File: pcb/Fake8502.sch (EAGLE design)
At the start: 16 parts, among them IC2 XC9572XLTQG100, IC5 HDR, IC6 65(C)02

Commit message: Fixed port definitions
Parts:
- removed IC5: HDR, commodore:8502-RP
- removed IC6: 65(C)02, commodore:6502-RP
- added IC1: W65C02SP, commodore:W65C02SP-R
- added IC3: XC9572XLTQG100, xilinx_xc95XXXxl:XC9572XLTQG100
- added SJ1: (no value), jumper:SJ
- IC2: value XC9572XLTQG100 -> MOS8502; device xilinx_xc95XXXxl:XC9572XLTQG100 -> commodore:8502-RP
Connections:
- removed net !RDY': IC2.FB1MC15, IC6A.!RDY
- new net N$1: IC1A.!VP, SJ1.2
- net !IRQ: now also IC1A.!IRQ, IC2>NAME.!IRQ, IC3.FB1MC17; no longer IC2.FB1MC17, IC5>NAME.!IRQ, IC6A.!IRQ
- net !NMI: now also IC1A.!NMI, IC2>NAME.!NMI, IC3.FB3MC2; no longer IC2.FB3MC2, IC5>NAME.!NMI, IC6A.!NMI
- net !RDY: now also IC1A.!RDY, IC2>NAME.!RDY, IC3.FB1MC10; no longer IC2.FB1MC10, IC5>NAME.!RDY
- net !RESET: now also IC1A.!RESET, IC2>NAME.!RESET, IC3.FB2MC9-I/O/GSR; no longer IC2.FB2MC9-I/O/GSR, IC5>NAME.!RESET, IC6A.!RESET
- net +3V3: now also IC3.VCCINT3,3V@1, IC3.VCCINT3,3V@2, IC3.VCCINT3,3V@3, IC3.VCCIO2,5V/3,3V@1, IC3.VCCIO2,5V/3,3V@2, IC3.VCCIO2,5V/3,3V@3, IC3.VCCIO2,5V/3,3V@4; no longer IC2.VCCINT3,3V@1, IC2.VCCINT3,3V@2, IC2.VCCINT3,3V@3, IC2.VCCIO2,5V/3,3V@1, IC2.VCCIO2,5V/3,3V@2, IC2.VCCIO2,5V/3,3V@3, IC2.VCCIO2,5V/3,3V@4
- net A'0: now also IC1A.A0, IC3.FB1MC4; no longer IC2.FB1MC4, IC6A.A0
- net A'1: now also IC1A.A1, IC3.FB1MC8; no longer IC2.FB1MC8, IC6A.A1
- net A'10: now also IC1A.A10, IC3.FB3MC15; no longer IC2.FB3MC15, IC6A.A10
- net A'11: now also IC1A.A11, IC3.FB3MC18; no longer IC2.FB3MC18, IC6A.A11
- net A'12: now also IC1A.A12, IC3.FB4MC3; no longer IC2.FB4MC3, IC6A.A12
- net A'13: now also IC1A.A13, IC3.FB4MC11; no longer IC2.FB4MC11, IC6A.A13
- net A'14: now also IC1A.A14, IC3.FB4MC7; no longer IC2.FB4MC7, IC6A.A14
- net A'15: now also IC1A.A15, IC3.FB4MC18; no longer IC2.FB4MC18, IC6A.A15
- net A'2: now also IC1A.A2, IC3.FB1MC6; no longer IC2.FB1MC6, IC6A.A2
- net A'3: now also IC1A.A3, IC3.FB1MC12; no longer IC2.FB1MC12, IC6A.A3
- net A'4: now also IC1A.A4, IC3.FB1MC13; no longer IC2.FB1MC13, IC6A.A4
- net A'5: now also IC1A.A5, IC3.FB1MC16; no longer IC2.FB1MC16, IC6A.A5
- net A'6: now also IC1A.A6, IC3.FB3MC1; no longer IC2.FB3MC1, IC6A.A6
- net A'7: now also IC1A.A7, IC3.FB3MC3; no longer IC2.FB3MC3, IC6A.A7
- net A'8: now also IC1A.A8, IC3.FB3MC11; no longer IC2.FB3MC11, IC6A.A8
- net A'9: now also IC1A.A9, IC3.FB3MC7; no longer IC2.FB3MC7, IC6A.A9
- net A0: now also IC2>NAME.A0, IC3.FB1MC10-I/O/GCK2; no longer IC2.FB1MC10-I/O/GCK2, IC5>NAME.A0
- net A1: now also IC2>NAME.A1, IC3.FB1MC9-I/O/GCK1; no longer IC2.FB1MC9-I/O/GCK1, IC5>NAME.A1
- net A10: now also IC2>NAME.A10, IC3.FB3MC6; no longer IC2.FB3MC6, IC5>NAME.A10
- net A11: now also IC2>NAME.A11, IC3.FB3MC14; no longer IC2.FB3MC14, IC5>NAME.A11
- net A12: now also IC2>NAME.A12, IC3.FB3MC17; no longer IC2.FB3MC17, IC5>NAME.A12
- net A13: now also IC2>NAME.A13, IC3.FB3MC10; no longer IC2.FB3MC10, IC5>NAME.A13
- net A14: now also IC2>NAME.A14, IC3.FB4MC4; no longer IC2.FB4MC4, IC5>NAME.A14
- net A15: now also IC2>NAME.A15, IC3.FB4MC6; no longer IC2.FB4MC6, IC5>NAME.A15
- net A2: now also IC2>NAME.A2, IC3.FB1MC3; no longer IC2.FB1MC3, IC5>NAME.A2
- net A3: now also IC2>NAME.A3, IC3.FB1MC1; no longer IC2.FB1MC1, IC5>NAME.A3
- net A4: now also IC2>NAME.A4, IC3.FB1MC5; no longer IC2.FB1MC5, IC5>NAME.A4
- net A5: now also IC2>NAME.A5, IC3.FB3MC5; no longer IC2.FB3MC5, IC5>NAME.A5
- net A6: now also IC2>NAME.A6, IC3.FB3MC8; no longer IC2.FB3MC8, IC5>NAME.A6
- net A7: now also IC2>NAME.A7, IC3.FB1MC18; no longer IC2.FB1MC18, IC5>NAME.A7
- net A8: now also IC2>NAME.A8, IC3.FB3MC9; no longer IC2.FB3MC9, IC5>NAME.A8
- net A9: now also IC2>NAME.A9, IC3.FB3MC4; no longer IC2.FB3MC4, IC5>NAME.A9
- net AEC: now also IC2>NAME.AEC, IC3.FB1MC7; no longer IC2.FB1MC7, IC5>NAME.AEC
- net D'0: now also IC1A.D0, IC3.FB2MC13; no longer IC2.FB2MC13, IC6A.D0
- net D'1: now also IC1A.D1, IC3.FB2MC16; no longer IC2.FB2MC16, IC6A.D1
- net D'2: now also IC1A.D2, IC3.FB2MC17; no longer IC2.FB2MC17, IC6A.D2
- net D'3: now also IC1A.D3, IC3.FB2MC4; no longer IC2.FB2MC4, IC6A.D3
- net D'4: now also IC1A.D4, IC3.FB2MC3; no longer IC2.FB2MC3, IC6A.D4
- net D'5: now also IC1A.D5, IC3.FB4MC15; no longer IC2.FB4MC15, IC6A.D5
- net D'6: now also IC1A.D6, IC3.FB4MC16; no longer IC2.FB4MC16, IC6A.D6
- net D'7: now also IC1A.D7, IC3.FB4MC12; no longer IC2.FB4MC12, IC6A.D7
- net D0: now also IC2>NAME.D0, IC3.FB2MC6; no longer IC2.FB2MC6, IC5>NAME.D0
- net D1: now also IC2>NAME.D1, IC3.FB2MC5; no longer IC2.FB2MC5, IC5>NAME.D1
- net D2: now also IC2>NAME.D2, IC3.FB2MC2; no longer IC2.FB2MC2, IC5>NAME.D2
- net D3: now also IC2>NAME.D3, IC3.FB2MC10; no longer IC2.FB2MC10, IC5>NAME.D3
- net D4: now also IC2>NAME.D4, IC3.GTS1; no longer IC2.GTS1, IC5>NAME.D4
- net D5: now also IC2>NAME.D5, IC3.FB2MC12; no longer IC2.FB2MC12, IC5>NAME.D5
- net D6: now also IC2>NAME.D6, IC3.FB2MC14; no longer IC2.FB2MC14, IC5>NAME.D6
- net D7: now also IC2>NAME.D7, IC3.FB2MC15; no longer IC2.FB2MC15, IC5>NAME.D7
- net GND: now also IC1P.GND, IC2P.GND, IC3.GND@1, IC3.GND@2, IC3.GND@3, IC3.GND@4, IC3.GND@5, IC3.GND@6, IC3.GND@7, IC3.GND@8, SJ1.1; no longer IC2.GND@1, IC2.GND@2, IC2.GND@3, IC2.GND@4, IC2.GND@5, IC2.GND@6, IC2.GND@7, IC2.GND@8, IC5P.GND, IC6P.GND, IC6P.GND@1
- net N$3: now also IC3.TCK; no longer IC2.TCK
- net N$4: now also IC3.TMS; no longer IC2.TMS
- net N$5: now also IC3.TDI; no longer IC2.TDI
- net N$6: now also IC3.TDO; no longer IC2.TDO
- net P0: now also IC2>NAME.P0, IC3.FB1MC2; no longer IC2.FB1MC2, IC5>NAME.P0
- net P1: now also IC2>NAME.P1, IC3.FB2MC18; no longer IC2.FB2MC18, IC5>NAME.P1
- net P2: now also IC2>NAME.P2, IC3.FB4MC17; no longer IC2.FB4MC17, IC5>NAME.P2
- net P3: now also IC2>NAME.P3, IC3.FB2MC1; no longer IC2.FB2MC1, IC5>NAME.P3
- net P4: now also IC2>NAME.P4, IC3.FB4MC13; no longer IC2.FB4MC13, IC5>NAME.P4
- net P5: now also IC2>NAME.P5, IC3.FB4MC10; no longer IC2.FB4MC10, IC5>NAME.P5
- net P6: now also IC2>NAME.P6, IC3.FB4MC14; no longer IC2.FB4MC14, IC5>NAME.P6
- net PHI: now also IC1A.PHI0, IC2>NAME.PHI0, IC3.FB1MC14-I/O/GCK3; no longer IC2.FB1MC14-I/O/GCK3, IC5>NAME.PHI0, IC6A.PHI0
- net R/!W: now also IC2>NAME.R/!W, IC3.FB2MC8; no longer IC2.FB2MC8, IC5>NAME.R/!W
- net R/!W': now also IC1A.R/!W, IC3.FB2MC11-I/O/GTS2; no longer IC2.FB2MC11-I/O/GTS2, IC6A.R/!W
- net VCC: now also IC1P.VCC, IC2P.VCC; no longer IC5P.VCC, IC6P.VCC

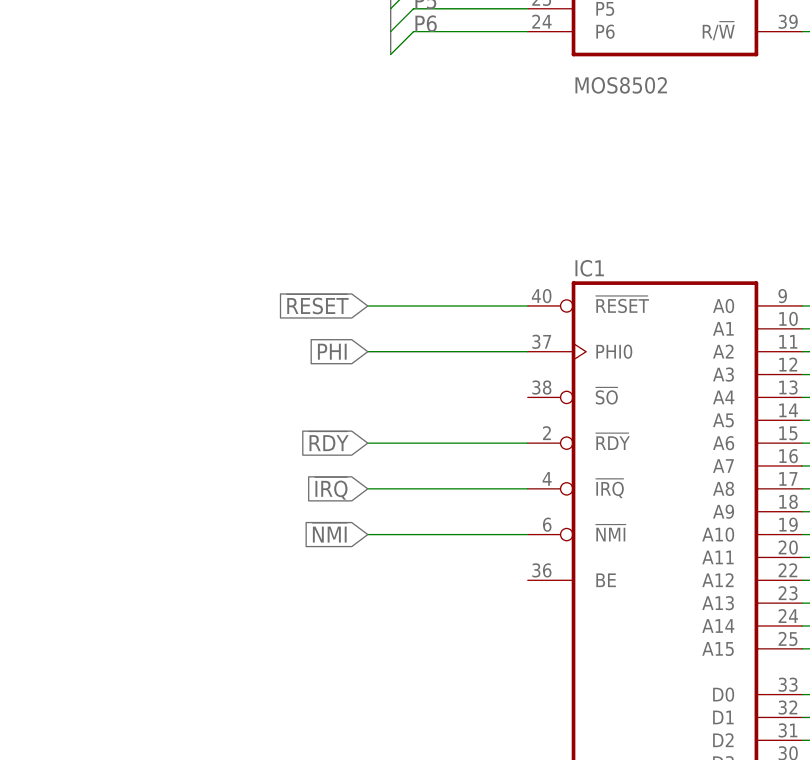
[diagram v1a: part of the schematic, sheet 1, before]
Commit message: Created GFX for schematic and PCB
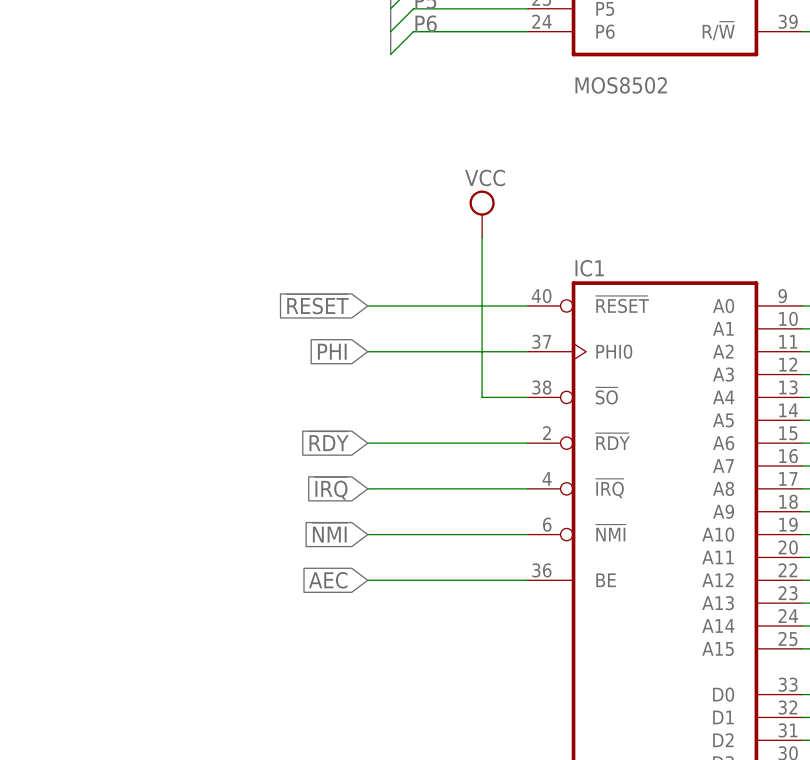
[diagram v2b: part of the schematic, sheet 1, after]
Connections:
- net AEC: now also IC1A.BE
- net VCC: now also IC1A.!SO
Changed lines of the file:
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@@
 <part name="IC1" library="commodore" deviceset="W65C02SP" device="-R" value="W65C02SP"/>
 <part name="SJ1" library="jumper" deviceset="SJ" device=""/>
+<part name="SUPPLY4" library="supply2" deviceset="VCC" device=""/>
 </parts>
 <sheets>
 <sheet>
+<description>CPU</description>
 <plain>
 </plain>
@@
 <instance part="IC1" gate="P" x="12.7" y="20.32"/>
 <instance part="SJ1" gate="1" x="220.98" y="43.18" rot="R90"/>
+<instance part="SUPPLY4" gate="G$1" x="182.88" y="152.4"/>
 </instances>
 <busses>
@@
 <label x="170.18" y="223.52" size="1.778" layer="95" rot="R180" xref="yes"/>
 </segment>
+<segment>
+<wire x1="170.18" y1="111.76" x2="187.96" y2="111.76" width="0.1524" layer="91"/>
+<pinref part="IC1" gate="A" pin="BE"/>
+<label x="170.18" y="111.76" size="1.778" layer="95" rot="R180" xref="yes"/>
+</segment>
 </net>
 <net name="P0" class="0">
@@
 <pinref part="IC1" gate="P" pin="VCC"/>
 </segment>
+<segment>
+<pinref part="IC1" gate="A" pin="!SO"/>
+<wire x1="187.96" y1="132.08" x2="182.88" y2="132.08" width="0.1524" layer="91"/>
+<wire x1="182.88" y1="132.08" x2="182.88" y2="149.86" width="0.1524" layer="91"/>
+<pinref part="SUPPLY4" gate="G$1" pin="VCC"/>
+</segment>
 </net>
 <net name="GND" class="0">
@@
 </sheet>
 <sheet>
+<description>LOGIC</description>
 <plain>
 </plain>
@@
 <wire x1="254" y1="187.96" x2="251.46" y2="190.5" width="0.1524" layer="91"/>
 <wire x1="251.46" y1="190.5" x2="238.76" y2="190.5" width="0.1524" layer="91"/>
-<label x="251.46" y="190.5" size="1.778" layer="95" rot="R180"/>
+<label x="251.46" y="190.5" size="1.778" layer="95" rot="MR0"/>
 <pinref part="IC3" gate="G$1" pin="FB4MC11"/>
 </segment>
@@
 <wire x1="259.08" y1="177.8" x2="256.54" y2="180.34" width="0.1524" layer="91"/>
 <wire x1="256.54" y1="180.34" x2="238.76" y2="180.34" width="0.1524" layer="91"/>
-<label x="251.46" y="180.34" size="1.778" layer="95" rot="R180"/>
+<label x="251.46" y="180.34" size="1.778" layer="95" rot="MR0"/>
 <pinref part="IC3" gate="G$1" pin="FB4MC4"/>
 </segment>
@@
 <wire x1="254" y1="172.72" x2="251.46" y2="175.26" width="0.1524" layer="91"/>
 <wire x1="251.46" y1="175.26" x2="238.76" y2="175.26" width="0.1524" layer="91"/>
-<label x="251.46" y="175.26" size="1.778" layer="95" rot="R180"/>
+<label x="251.46" y="175.26" size="1.778" layer="95" rot="MR0"/>
 <pinref part="IC3" gate="G$1" pin="FB4MC3"/>
 </segment>
@@
 <wire x1="124.46" y1="38.1" x2="127" y2="40.64" width="0.1524" layer="91"/>
 <wire x1="127" y1="40.64" x2="127" y2="50.8" width="0.1524" layer="91"/>
+<label x="127" y="40.64" size="1.778" layer="95" rot="R90"/>
 </segment>
 </net>
@@
 </sheet>
 <sheet>
+<description>POWER</description>
 <plain>
 </plain>
